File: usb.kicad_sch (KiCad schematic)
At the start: 80 parts, among them J1 USB_C_Receptacle_USB2.0, J2 USB_C_Receptacle_USB2.0, J3 USB_C_Receptacle_USB2.0, J4 USB_C_Receptacle_USB2.0, U1 MIMX8MM6DVTLZAA, U10 D5V0H1B2LP, U11 TPD4E02B04, U12 TPD4E02B04, U13 74LVC2G07, U14 D5V0H1B2LP, U15 CH343P, U16 TPD4E02B04, U17 INA231, U18 D5V0H1B2LP, U19 TS3USB221E, U20 TPD4E02B04, U4 74LVC2G04, U5 NX5P3363, U6 TUSB320LAI, U7 NX5P3363, U8 TUSB320LAI, U9 D5V0H1B2LP

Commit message: pmic routing almost done
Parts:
- C102, C103: footprint Capacitor_SMD:C_0603_1608Metric -> qsbc:C_0603_1608Metric
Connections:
- net USB4_VBUS: no longer U17.D1 (Vbus)
- net VSYS_5V: now also U17.D1 (Vbus)
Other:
- moved on the sheet: R41, U17

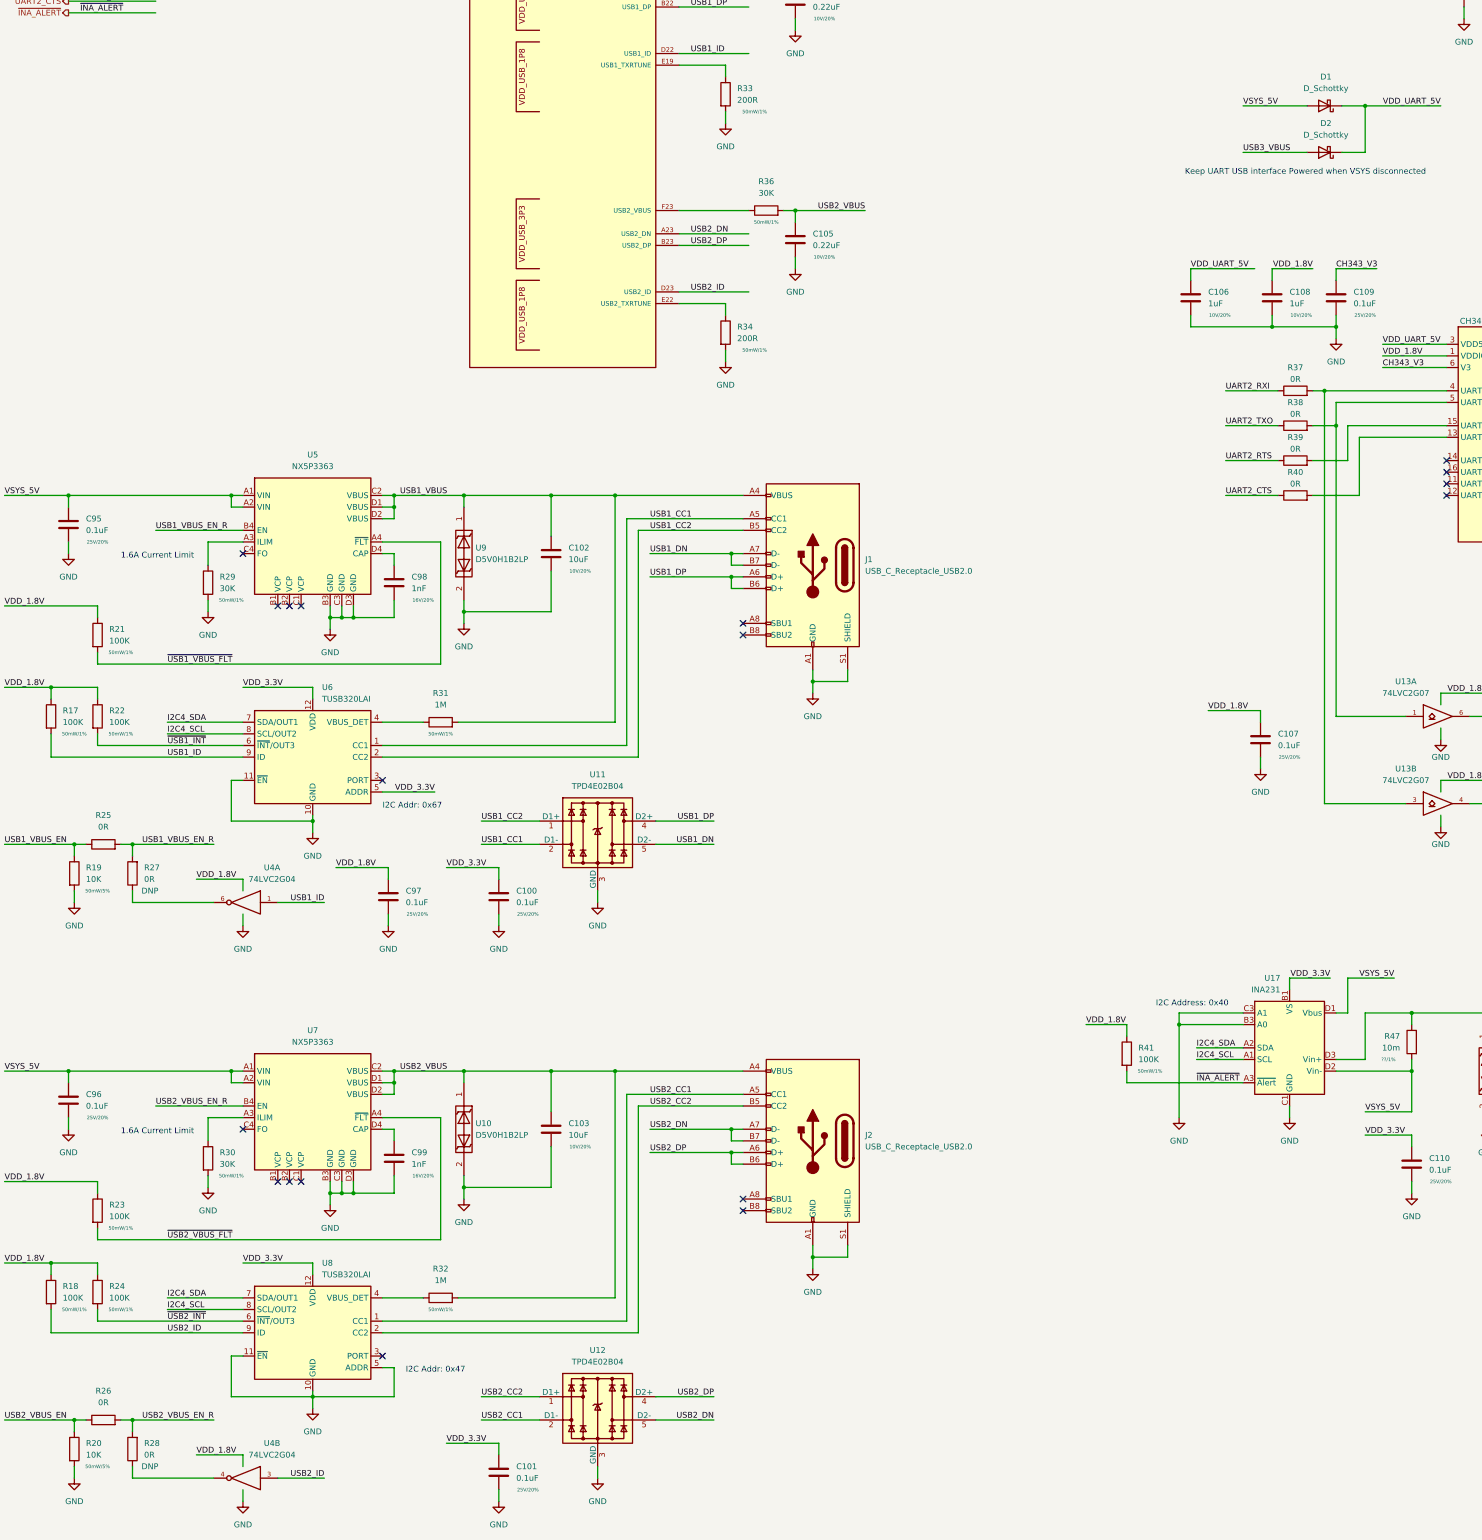
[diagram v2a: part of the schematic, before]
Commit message: bom work, change uart level shifter and m.2 socket
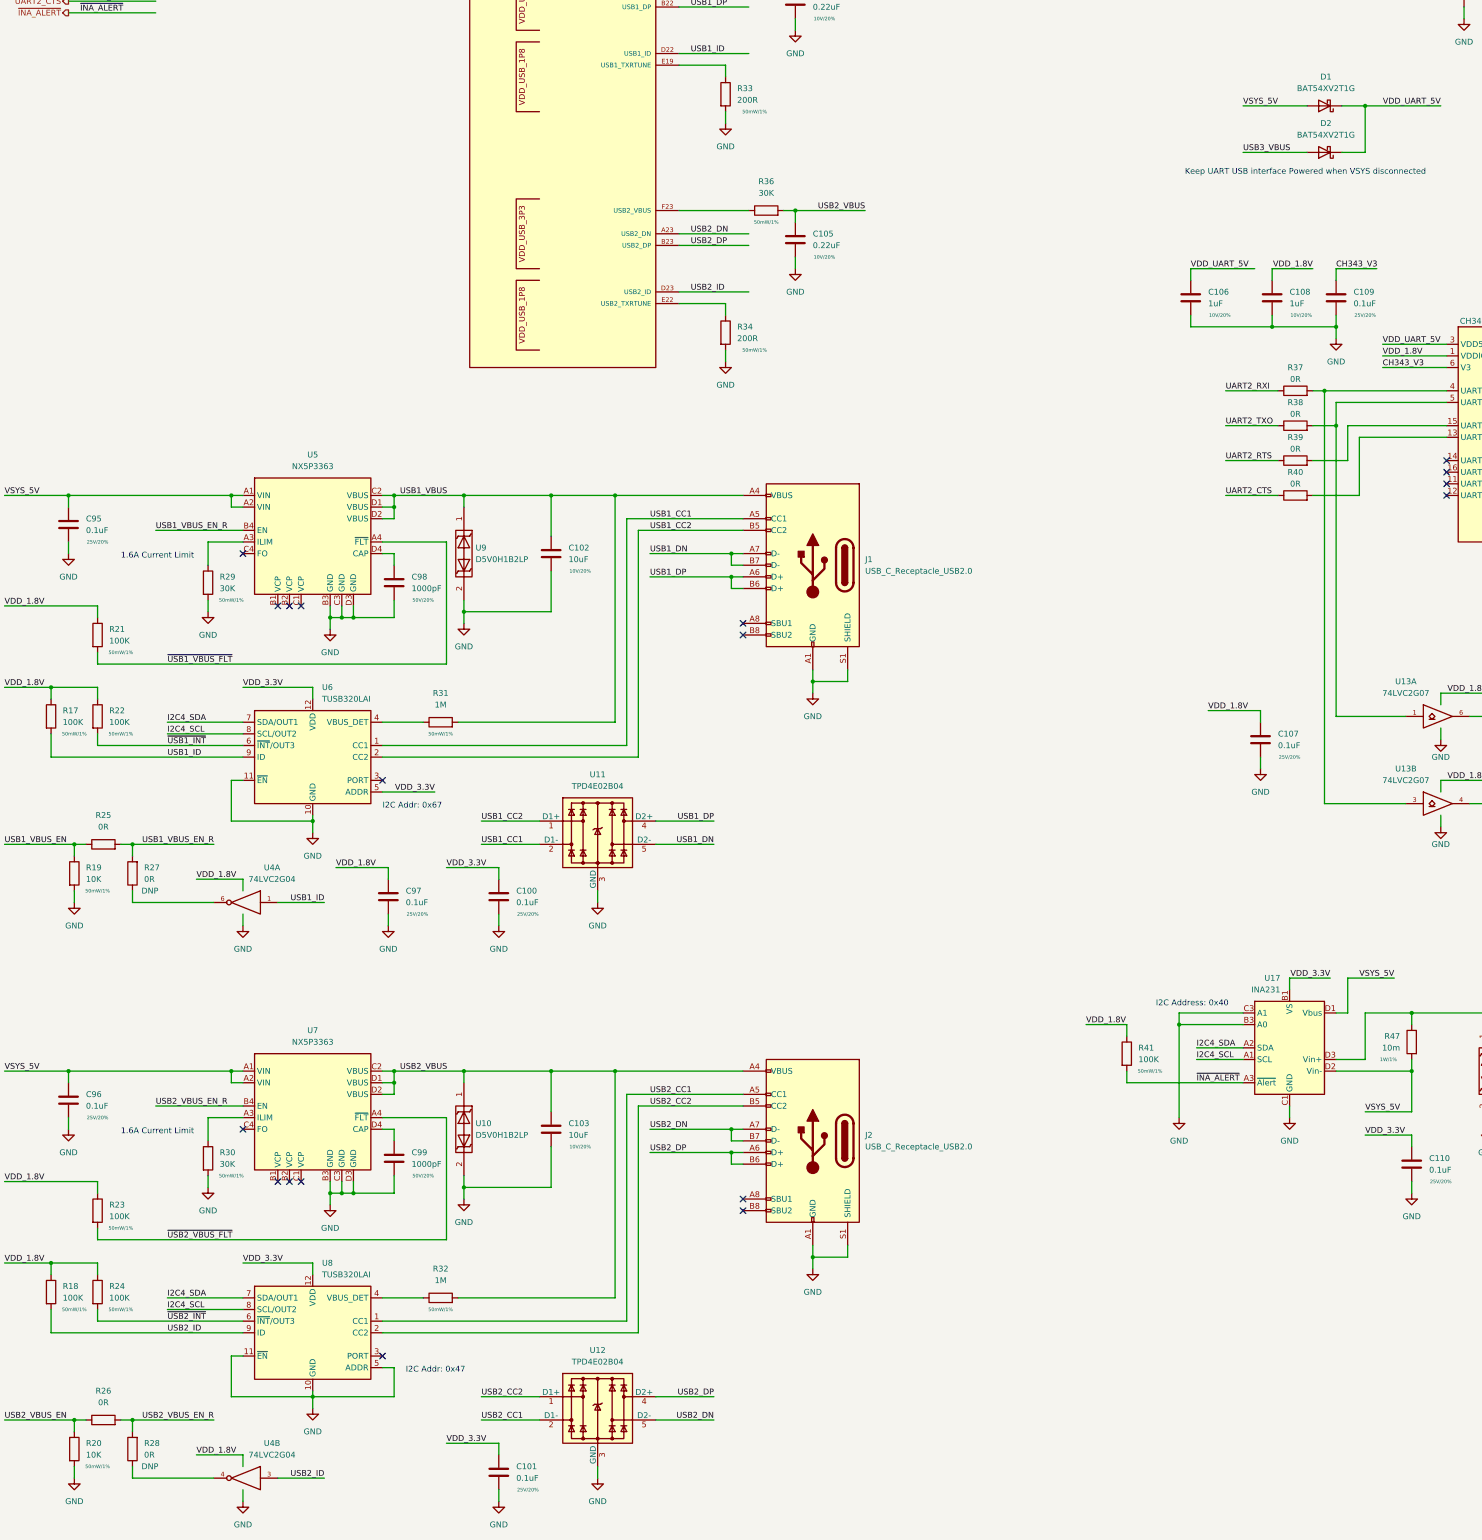
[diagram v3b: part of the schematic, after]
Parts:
- C100, C101, C107, C109, C110, C111, C95, C96, C97: MPN (none) -> CL05A104KA5NNNC
- C102, C103: MPN (none) -> CL10A106KP8NNNC
- C104, C105: MPN (none) -> GRM033R61A224KE90D
- C106, C108: MPN (none) -> CL05A105KP5NNNC
- C98, C99: value 1nF -> 1000pF; MPN (none) -> GRM1555C1H102JA01D; Rating 16V/20% -> 50V/20%
- D1, D2: value D_Schottky -> BAT54XV2T1G; MPN (none) -> BAT54XV2T1G
- D3: MPN (none) -> SML-E12Y8WT86
- D4: MPN (none) -> SML-E12D8WT86
- J1, J2, J4: MPN (none) -> USB4105-GF-A
- J3: MPN (none) -> KUSBX-SL-CS1N14-B
- R17, R18, R21, R22, R23, R24, R41: MPN (none) -> RC0402FR-07100KL
- R19, R20: MPN (none) -> RC0402FR-0710KL; Rating 50mW/5% -> 50mW/1%
- R25, R26, R27, R28, R37, R38, R39, R40, R48: MPN (none) -> RC0402FR-070RL
- R29, R30, R35, R36: MPN (none) -> RC0201FR-0730KL
- R31, R32: MPN (none) -> RC0402FR-071ML
- R33, R34: MPN (none) -> RC0402FR-07200RL
- R42, R44, R51, R52: MPN (none) -> RC0402FR-075K1L
- R43, R46: MPN (none) -> RC0402FR-072K2L
- R45, R49, R50: MPN (none) -> RC0402FR-0710KL
- R47: MPN (none) -> ERJ-8CWFR010V; Rating ??/1% -> 1W/1%
- U1: MPN (none) -> MIMX8MM6DVTLZAA
- U10, U14, U18, U9: MPN (none) -> D5V0H1B2LP-7B
- U11, U12, U16, U20: MPN (none) -> TPD4E02B04DQAR
- U13: MPN (none) -> 74LVC2G07FZ4-7
- U15: MPN (none) -> CH343P
- U17: MPN (none) -> INA231AIYFFR
- U19: MPN (none) -> TS3USB221ERSER
- U4: footprint Package_TO_SOT_SMD:SOT-886 -> Package_TO_SOT_SMD:SOT-363_SC-70-6; MPN (none) -> SN74LVC2G04DCKR
- U5, U7: MPN (none) -> NX5P3363UKZ
- U6, U8: MPN (none) -> TUSB320LAIRWBR

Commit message: ddr length matching work, misc cleanup
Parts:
- renumbered C101 to C100, C102 to C101, C103 to C102, C104 to C103, C105 to C104, C106 to C105, C107 to C106, C108 to C107, C109 to C108, C110 to C109, C111 to C110, C95 to C94, C96 to C95, C97 to C96, C98 to C97, C99 to C98, C100 to C99, R41 to R37, R37 to R38, R38 to R39, R39 to R40, R40 to R41, R47 to R42, R42 to R43, R51 to R44, R43 to R45, R44 to R46, R45 to R47, R52 to R48, R46 to R49, R48 to R50, R49 to R51, R50 to R52, U17 to U13, U13 to U14, U14 to U15, U18 to U16, U15 to U17, U16 to U18, U20 to U19, U19 to U20

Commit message: misc cleanup, change from usb mux to dual uart
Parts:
- removed D1, D2: BAT54XV2T1G, Diode_SMD:D_SOD-523, symbol Device:D_Schottky
- removed R50: 0R, qsbc:R_0402_1005Metric, symbol Device:R
- removed R51: 10K, qsbc:R_0402_1005Metric, symbol Device:R
- removed U20: TS3USB221E, Package_DFN_QFN:Texas_R-PUQFN-N10, symbol qsbc:TS3USB221E
- added C111, C113: 0.1uF, qsbc:C_0402_1005Metric, symbol Device:C
- added C112: 1uF, qsbc:C_0402_1005Metric, symbol Device:C
- added D3: LED_Yellow, LED_SMD:LED_0603_1608Metric, symbol Device:LED
- added D4: LED_Orange, LED_SMD:LED_0603_1608Metric, symbol Device:LED
- added R37, R38, R53, R54, R55: 0R, qsbc:R_0402_1005Metric, symbol Device:R
- added R56, R58: 2.2K, qsbc:R_0402_1005Metric, symbol Device:R
- added R57: 10K, qsbc:R_0402_1005Metric, symbol Device:R
- added U20: 74LVC2G07, Package_TO_SOT_SMD:SOT-886, symbol 74xGxx:74LVC2G07
- added U21: CH343P, Package_DFN_QFN:QFN-16-1EP_3x3mm_P0.5mm_EP1.45x1.45mm_ThermalVias, symbol qsbc:CH343P
- C110: value 0.1uF -> 1uF; MPN CL05A104KA5NNNC -> CL05A105KP5NNNC; Rating 25V/20% -> 10V/20%
- R52: value 10K -> 0R; MPN RC0402FR-0710KL -> RC0402FR-070RL; Rating 50mW/1% -> (none)
- TP21: now left out of the parts list
- U6, U8: value TUSB320LAI -> TUSB320LI; MPN TUSB320LAIRWBR -> TUSB320LIRWBR
- renumbered D3 to D1, D4 to D2, R37 to R39, R38 to R40, R39 to R41, R40 to R42, R41 to R43, R42 to R44, R43 to R45, R44 to R46, R45 to R47, R46 to R48, R47 to R49, R48 to R50, R49 to R51
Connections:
- net USBUART_DN is gone; now on net USB3_DN: U17.8 (USB_DN)
- net USBUART_DP is gone; now on net USB3_DP: U17.7 (USB_DP)
- net VDD_UART_5V is gone; now on net USB3_VBUS: C105.1, U17.3 (VDD5), U17.9 (USB_VBUS)
- net GND: now also C111.2, C112.2, C113.2, R57.2, U20.2 (GND), U20.2 (GND), U21.17 (EPAD), U21.2 (GND); no longer R52.2
- net USB1_ID: now also R37.2; no longer U1.D22 (USB1_ID)
- net USB2_ID: now also R38.2; no longer U1.D23 (USB2_ID)
- net USB3_DN: now also U18.1 (D1+), U18.10; no longer U18.2 (D1-), U18.9
- net USB3_DP: now also U18.2 (D1-), U18.9; no longer U18.1 (D1+), U18.10
- net USB4_DN: now also U21.8 (USB_DN)
- net USB4_DP: now also U21.7 (USB_DP)
- net VCC: now also C111.1, C112.1, U20.5 (VCC), U20.5 (VCC), U21.1 (VDDIO)
- net VDD_3.3V: now also R56.1, R58.1
- net VSYS_5V: now also C110.1, U21.3 (VDD5), U21.9 (USB_VBUS)
- net UART1_RXI: now reaches R52.1
- net CH343_V3 renamed CH343_V3_1
- net CH343_V3_1: no longer C110.1
- new net: R57.1, U21.10 (~{ACT})
- new net: R55.2, U21.13 (UART_RTS)
- new net: R54.2, U21.15 (UART_CTS)
- new net: R52.2, U20.3, U21.4 (UART_TXD)
- new net: R53.2, U20.1, U21.5 (UART_RXD)
- new net: D4.1 (K), U20.4
- new net: D4.2 (A), R58.2
- new net: D3.2 (A), R56.2
- new net: D3.1 (K), U20.6
- new net CH343_V3_2: C113.1, U21.6 (V3)
- new net UART1_CTS: R55.1
- new net UART1_RTS: R54.1
- new net UART1_TXO: R53.1
- new net USB1_ID_R: R37.1, U1.D22 (USB1_ID)
- new net USB2_ID_R: R38.1, U1.D23 (USB2_ID)
- no-connect marks 26 -> 30
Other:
- note removed: "Keep UART USB interface Powered when VSYS disconnected"

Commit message: Rev 1
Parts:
- added C110: 0.1uF, qsbc:C_0402_1005Metric, symbol Device:C
- added TP22: TestPoint, TestPoint:TestPoint_Pad_D1.0mm, symbol Connector:TestPoint
- renumbered C110 to C111, C111 to C112, C112 to C113, C113 to C114, R47 to R46, R48 to R47, R49 to R48, R46 to R49, U17 to U16, U16 to U17
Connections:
- net GND: now also C110.2, TP22.1
- net USB4_VBUS: now also C110.1
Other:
- moved on the sheet: J4, R49, R50, TP21, U17, U19

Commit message: misc changes for rev1
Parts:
- R27, R28, R37, R38, R48, R57: now left out of the parts list
- R44: MPN ERJ-8CWFR010V -> ERJ8CWFR010V
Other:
- note added: "TODO: Add VDDIO LDO so USB-UART does not reset on board reset"
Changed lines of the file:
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@@
     (effects (font (size 1.27 1.27)) (justify left bottom))
   )
+  (text "TODO: Add VDDIO LDO so USB-UART\ndoes not reset on board reset"
+    (at 382.27 121.92 0)
+    (effects (font (size 1.27 1.27)) (justify left bottom))
+  )
   (text "1.6A Current Limit" (at 53.34 306.07 0)
     (effects (font (size 1.27 1.27)) (justify left bottom))
@@
   )
   (symbol (lib_id "Device:R") (at 55.88 248.92 180) (unit 1)
-    (in_bom yes) (on_board yes)
+    (in_bom no) (on_board yes)
     (property "Reference" "R27" (id 0) (at 58.42 247.6499 0)
       (effects (font (size 1.27 1.27)) (justify right))
@@
   )
   (symbol (lib_id "Device:R") (at 215.9 121.92 90) (unit 1)
-    (in_bom yes) (on_board yes) (fields_autoplaced)
+    (in_bom no) (on_board yes)
     (property "Reference" "R38" (id 0) (at 215.9 115.57 90))
     (property "Value" "0R" (id 1) (at 215.9 118.11 90))
@@
   )
   (symbol (lib_id "Device:R") (at 215.9 69.85 90) (unit 1)
-    (in_bom yes) (on_board yes) (fields_autoplaced)
+    (in_bom no) (on_board yes)
     (property "Reference" "R37" (id 0) (at 215.9 63.5 90))
     (property "Value" "0R" (id 1) (at 215.9 66.04 90))
@@
   )
   (symbol (lib_id "Device:R") (at 378.46 160.02 0) (unit 1)
-    (in_bom yes) (on_board yes)
+    (in_bom no) (on_board yes)
     (property "Reference" "R48" (id 0) (at 381 158.7499 0)
       (effects (font (size 1.27 1.27)) (justify left))
@@
       (effects (font (size 0.762 0.762)))
     )
-    (property "MPN" "ERJ-8CWFR010V" (id 5) (at 335.28 285.75 0)
+    (property "MPN" "ERJ8CWFR010V" (id 5) (at 335.28 285.75 0)
       (effects (font (size 1.27 1.27)) hide)
     )
@@
   )
   (symbol (lib_id "Device:R") (at 55.88 374.65 180) (unit 1)
-    (in_bom yes) (on_board yes)
+    (in_bom no) (on_board yes)
     (property "Reference" "R28" (id 0) (at 58.42 373.3799 0)
       (effects (font (size 1.27 1.27)) (justify right))
@@
   )
   (symbol (lib_id "Device:R") (at 528.32 160.02 0) (unit 1)
-    (in_bom yes) (on_board yes)
+    (in_bom no) (on_board yes)
     (property "Reference" "R57" (id 0) (at 530.86 158.7499 0)
       (effects (font (size 1.27 1.27)) (justify left))
